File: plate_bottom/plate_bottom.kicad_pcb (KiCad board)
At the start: 2 copper layers, 178.4 x 118.1 mm, 12 parts

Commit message: WIP
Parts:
- moved HM5 2.92 mm to (95.5, 95.7)
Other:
- outline, holes or cut-outs redrawn
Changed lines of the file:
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@@
   (general
     (thickness 1.6)
-    (drawings 117)
+    (drawings 119)
     (tracks 0)
     (zones 0)
@@
   )
   (module used_footprints:Hole_Mount_M4 (layer F.Cu)
+    (at 95.45 95.65)
+    (fp_text reference HM5 (at -0.01 -2.09) (layer Dwgs.User) hide
+      (effects (font (size 1 1) (thickness 0.15)))
+    )
+    (fp_text value CaseHole (at 0.5 -3.77) (layer F.Fab) hide
+      (effects (font (size 1 1) (thickness 0.15)))
+    )
+    (pad "" np_thru_hole circle (at 0 0.08168) (size 2.2 2.2) (drill 2.2) (layers *.Cu *.Mask))
+  )
+  (module used_footprints:Hole_Mount_M4 (layer F.Cu)
     (at 215.4 123.65 36)
     (fp_text reference HM1 (at -0.01 -2.09 36) (layer F.SilkS) hide
@@
   )
   (module used_footprints:Hole_Mount_M4 (layer F.Cu)
-    (at 95.5 98.56832)
-    (fp_text reference HM5 (at -0.01 -2.09) (layer Dwgs.User) hide
-      (effects (font (size 1 1) (thickness 0.15)))
-    )
-    (fp_text value CaseHole (at 0.5 -3.77) (layer F.Fab) hide
-      (effects (font (size 1 1) (thickness 0.15)))
-    )
-    (pad "" np_thru_hole circle (at 0 0.08168) (size 2.2 2.2) (drill 2.2) (layers *.Cu *.Mask))
-  )
-  (module used_footprints:Hole_Mount_M4 (layer F.Cu)
     (at 191.2725 55.183451 14.5)
     (fp_text reference HM2 (at -0.01 -2.09 14.5) (layer Dwgs.User) hide
@@
     (pad "" np_thru_hole circle (at 0 0) (size 2.2 2.2) (drill 2.2) (layers *.Cu *.Mask))
   )
+  (gr_arc (start 77.55 83.01) (end 77.55 82.01) (angle -90) (layer Edge.Cuts) (width 0.05))
+  (gr_arc (start 93.600001 83.01) (end 94.600001 83.01) (angle -90) (layer Edge.Cuts) (width 0.05))
+  (gr_line (start 93.6 100.84) (end 77.55 100.84) (layer Edge.Cuts) (width 0.05))
+  (gr_line (start 77.55 82.01) (end 93.600001 82.01) (layer Edge.Cuts) (width 0.05))
+  (gr_arc (start 77.55 99.84) (end 76.55 99.84) (angle -90) (layer Edge.Cuts) (width 0.05))
+  (gr_line (start 94.600001 83.01) (end 94.600001 84) (layer Edge.Cuts) (width 0.05))
+  (gr_line (start 76.55 99.84) (end 76.55 83.01) (layer Edge.Cuts) (width 0.05))
+  (gr_arc (start 95.099999 86.99) (end 95.599997 86.99) (angle -180) (layer Edge.Cuts) (width 0.05))
+  (gr_line (start 94.600001 92.589999) (end 94.600001 86.99) (layer Edge.Cuts) (width 0.05))
+  (gr_line (start 95.6 86.99) (end 95.599999 92.590001) (layer Edge.Cuts) (width 0.05))
+  (gr_arc (start 95.1 92.59) (end 94.600001 92.589999) (angle -180) (layer Edge.Cuts) (width 0.05))
+  (gr_arc (start 95.1 84) (end 94.600001 84) (angle -180) (layer Edge.Cuts) (width 0.05))
+  (gr_arc (start 93.6 99.84) (end 93.6 100.84) (angle -90) (layer Edge.Cuts) (width 0.05))
+  (gr_arc (start 95.1 98.84) (end 95.6 98.85) (angle -182.2915257) (layer Edge.Cuts) (width 0.05))
+  (gr_line (start 94.6 99.84) (end 94.6 98.85) (layer Edge.Cuts) (width 0.05))
   (gr_line (start 247.677579 53.038559) (end 227.4 56.25) (layer Edge.Cuts) (width 0.05))
   (gr_line (start 249.965825 54.701067) (end 254.95 86.2) (layer Edge.Cuts) (width 0.05))
@@
   (gr_line (start 234.283043 134.070973) (end 223.996802 148.22877) (layer Edge.Cuts) (width 0.05))
   (gr_line (start 96.6 117.55) (end 139.35 117.55) (layer Edge.Cuts) (width 0.05))
-  (gr_arc (start 95.500338 98.622885) (end 93.15 100.8) (angle -48.97400321) (layer Edge.Cuts) (width 0.05))
   (gr_line (start 134.05 52.950001) (end 141.35 52.950001) (layer Edge.Cuts) (width 0.05))
   (gr_line (start 133.05 53.950001) (end 133.05 59.5) (layer Edge.Cuts) (width 0.05))
@@
   (gr_line (start 170.55 30.55) (end 153.75 30.55) (layer Edge.Cuts) (width 0.05))
   (gr_line (start 152.75 31.55) (end 152.75 33.54) (layer Edge.Cuts) (width 0.05))
-  (gr_line (start 95.6 62) (end 95.599999 83.97) (layer Edge.Cuts) (width 0.05))
-  (gr_line (start 94.600001 82.97) (end 94.600001 83.97) (layer Edge.Cuts) (width 0.05))
-  (gr_line (start 76.55 99.8) (end 76.55 82.97) (layer Edge.Cuts) (width 0.05))
-  (gr_line (start 77.55 81.97) (end 93.600001 81.97) (layer Edge.Cuts) (width 0.05))
-  (gr_line (start 95.600014 101.825069) (end 95.6 116.55) (layer Edge.Cuts) (width 0.05))
+  (gr_line (start 95.6 62) (end 95.600099 84) (layer Edge.Cuts) (width 0.05))
+  (gr_line (start 95.6 98.85) (end 95.6 116.55) (layer Edge.Cuts) (width 0.05))
   (gr_arc (start 96.6 116.55) (end 95.6 116.55) (angle -90) (layer Edge.Cuts) (width 0.05))
-  (gr_arc (start 77.55 99.8) (end 76.55 99.8) (angle -90) (layer Edge.Cuts) (width 0.05))
-  (gr_arc (start 77.55 82.97) (end 77.55 81.97) (angle -90) (layer Edge.Cuts) (width 0.05))
-  (gr_arc (start 93.600001 82.97) (end 94.600001 82.97) (angle -90) (layer Edge.Cuts) (width 0.05))
   (gr_arc (start 96.6 42.59) (end 96.6 41.59) (angle -90) (layer Edge.Cuts) (width 0.05))
   (gr_arc (start 132.7 40.59) (end 132.7 41.59) (angle -90) (layer Edge.Cuts) (width 0.05))
@@
   (gr_arc (start 145.35 53.45) (end 145.35 52.950001) (angle -180) (layer Edge.Cuts) (width 0.05))
   (gr_arc (start 141.35 53.449999) (end 141.35 53.949997) (angle -180) (layer Edge.Cuts) (width 0.05))
-  (gr_arc (start 95.1 83.97) (end 94.600001 83.97) (angle -180) (layer Edge.Cuts) (width 0.05))
   (gr_arc (start 134.05 53.950001) (end 134.05 52.950001) (angle -90) (layer Edge.Cuts) (width 0.05))
   (gr_arc (start 153.6 50.45) (end 153.6 49.950001) (angle -90) (layer Edge.Cuts) (width 0.05))
@@
   (gr_line (start 96.6 60) (end 103.25 60.000001) (layer Edge.Cuts) (width 0.05))
   (gr_line (start 103.25 61) (end 96.6 61.000001) (layer Edge.Cuts) (width 0.05))
-  (gr_arc (start 95.099999 86.95) (end 95.599997 86.95) (angle -180) (layer Edge.Cuts) (width 0.05))
-  (gr_line (start 94.6 95.05) (end 94.600001 86.95) (layer Edge.Cuts) (width 0.05))
-  (gr_line (start 95.6 86.95) (end 95.599999 95.05) (layer Edge.Cuts) (width 0.05))
-  (gr_arc (start 95.1 95.049999) (end 94.600001 95.049998) (angle -180) (layer Edge.Cuts) (width 0.05))
-  (gr_line (start 93.15 100.8) (end 77.55 100.8) (layer Edge.Cuts) (width 0.05))
   (gr_line (start 227.4 56.25) (end 209.65 56.25) (layer Edge.Cuts) (width 0.05))
   (gr_line (start 191.7 55.25) (end 199 55.25) (layer Edge.Cuts) (width 0.05))

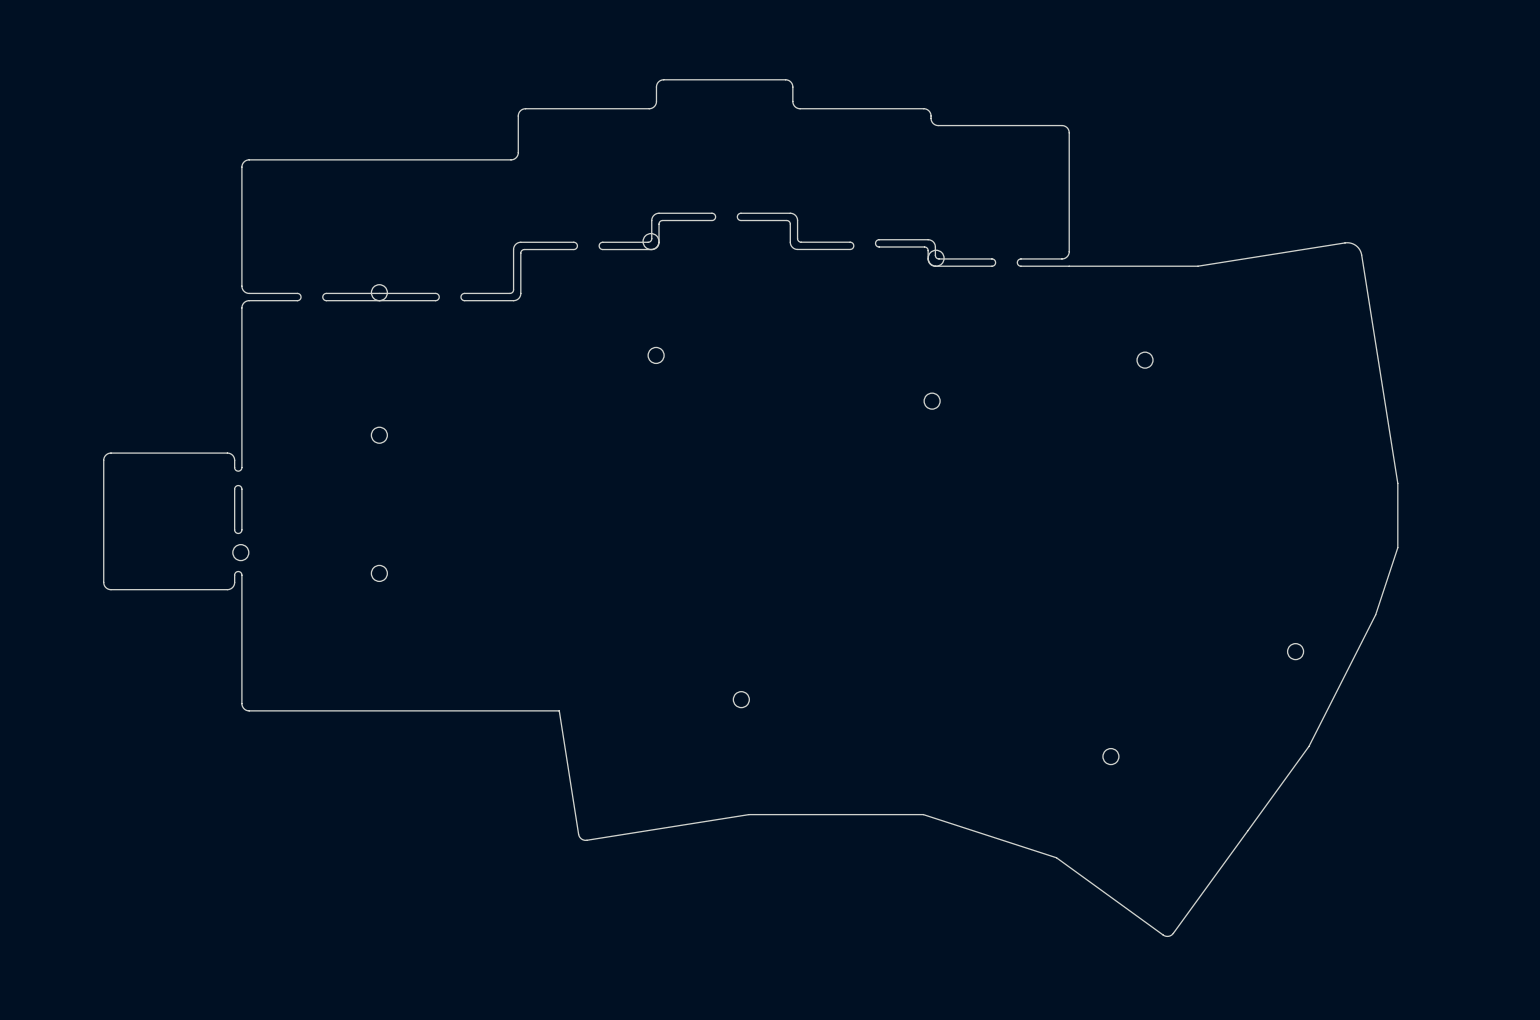
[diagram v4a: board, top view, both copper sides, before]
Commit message: Fixed cut edges + filled zones on plates.
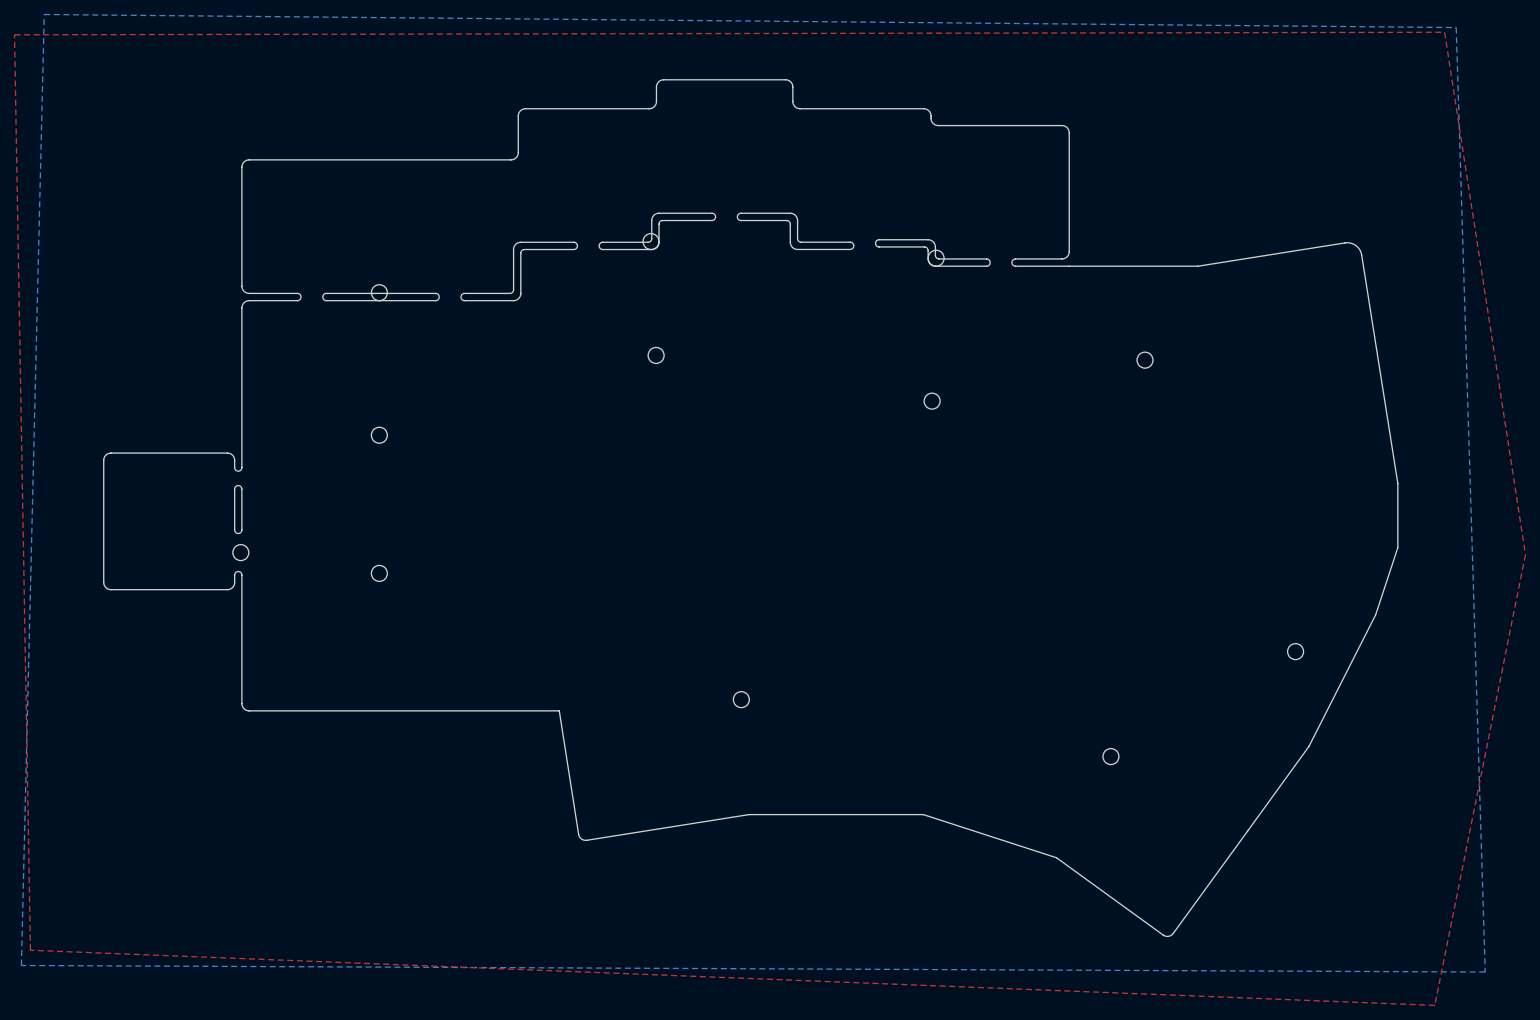
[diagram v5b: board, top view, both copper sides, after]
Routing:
- added copper zone on B.Cu, net (none)
- added copper zone on F.Cu, net (none)
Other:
- outline, holes or cut-outs redrawn
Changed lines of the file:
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@@
     (pad "" np_thru_hole circle (at 0 0) (size 2.2 2.2) (drill 2.2) (layers *.Cu *.Mask))
   )
+  (gr_line (start 191.2 56.25) (end 198.25 56.25) (layer Edge.Cuts) (width 0.05))
+  (gr_arc (start 202.25 55.749999) (end 202.25 55.25) (angle -180) (layer Edge.Cuts) (width 0.05))
+  (gr_arc (start 198.25 55.749998) (end 198.25 56.249996) (angle -180) (layer Edge.Cuts) (width 0.05))
+  (gr_line (start 191.7 55.25) (end 198.25 55.25) (layer Edge.Cuts) (width 0.05))
+  (gr_line (start 208.65 55.25) (end 202.25 55.25) (layer Edge.Cuts) (width 0.05))
   (gr_arc (start 77.55 83.01) (end 77.55 82.01) (angle -90) (layer Edge.Cuts) (width 0.05))
   (gr_arc (start 93.600001 83.01) (end 94.600001 83.01) (angle -90) (layer Edge.Cuts) (width 0.05))
@@
   (gr_line (start 183.45 53.6) (end 189.7 53.6) (layer Edge.Cuts) (width 0.05))
   (gr_line (start 190.2 54.1) (end 190.2 55.25) (layer Edge.Cuts) (width 0.05))
-  (gr_line (start 191.2 56.25) (end 199 56.249996) (layer Edge.Cuts) (width 0.05))
   (gr_line (start 209.65 54.25) (end 209.65 37.86) (layer Edge.Cuts) (width 0.05))
   (gr_line (start 208.65 36.86) (end 191.6 36.86) (layer Edge.Cuts) (width 0.05))
@@
   (gr_line (start 165.5 131.85) (end 189.55 131.85) (layer Edge.Cuts) (width 0.05))
   (gr_arc (start 134.55 54.449999) (end 134.55 53.95) (angle -90) (layer Edge.Cuts) (width 0.05))
-  (gr_line (start 203 56.249998) (end 209.65 56.25) (layer Edge.Cuts) (width 0.05))
-  (gr_line (start 208.65 55.25) (end 203 55.25) (layer Edge.Cuts) (width 0.05))
+  (gr_line (start 202.25 56.249998) (end 209.65 56.25) (layer Edge.Cuts) (width 0.05))
   (gr_arc (start 133.05 59.999999) (end 133.05 60.999999) (angle -90) (layer Edge.Cuts) (width 0.05))
   (gr_arc (start 122.3 60.499999) (end 122.3 60.999997) (angle -180) (layer Edge.Cuts) (width 0.05))
@@
   (gr_line (start 103.25 61) (end 96.6 61.000001) (layer Edge.Cuts) (width 0.05))
   (gr_line (start 227.4 56.25) (end 209.65 56.25) (layer Edge.Cuts) (width 0.05))
-  (gr_line (start 191.7 55.25) (end 199 55.25) (layer Edge.Cuts) (width 0.05))
-  (gr_arc (start 199 55.749998) (end 199 56.249996) (angle -180) (layer Edge.Cuts) (width 0.05))
-  (gr_arc (start 203 55.749999) (end 203 55.25) (angle -180) (layer Edge.Cuts) (width 0.05))
+  (zone (net 0) (net_name "") (layer F.Cu) (hatch edge 0.508)
+    (connect_pads (clearance 0.508))
+    (min_thickness 0.254)
+    (fill yes (arc_segments 32) (thermal_gap 0.508) (thermal_bridge_width 0.508))
+    (polygon
+      (pts
+        (xy 272.55 96) (xy 260.05 158.15) (xy 66.45 150.55) (xy 64.25 24.35) (xy 261.4 24)
+      )
+    )
+  )
+  (zone (net 0) (net_name "") (layer B.Cu) (hatch edge 0.508)
+    (connect_pads (clearance 0.508))
+    (min_thickness 0.254)
+    (fill yes (arc_segments 32) (thermal_gap 0.508) (thermal_bridge_width 0.508))
+    (polygon
+      (pts
+        (xy 263 23.35) (xy 267 153.55) (xy 65.2 152.65) (xy 68.35 21.55)
+      )
+    )
+  )
 )

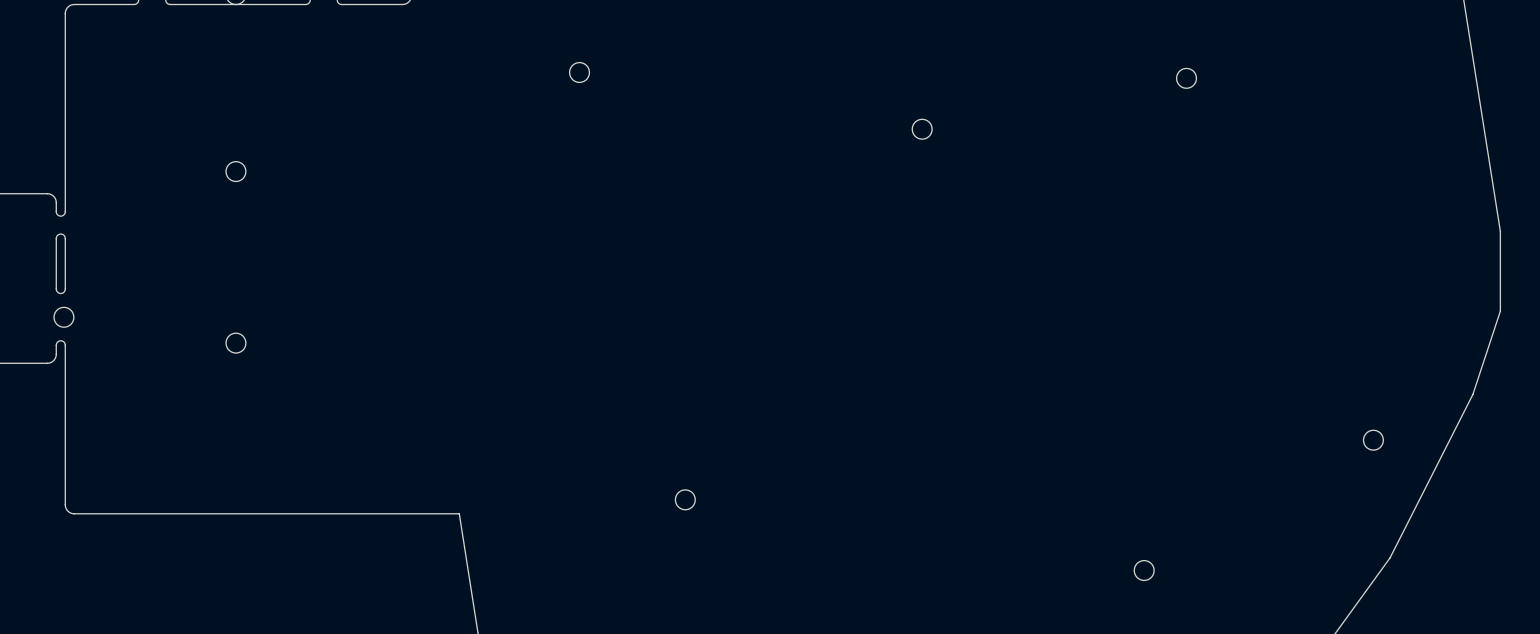
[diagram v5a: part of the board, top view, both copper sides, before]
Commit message: Added dimensions.
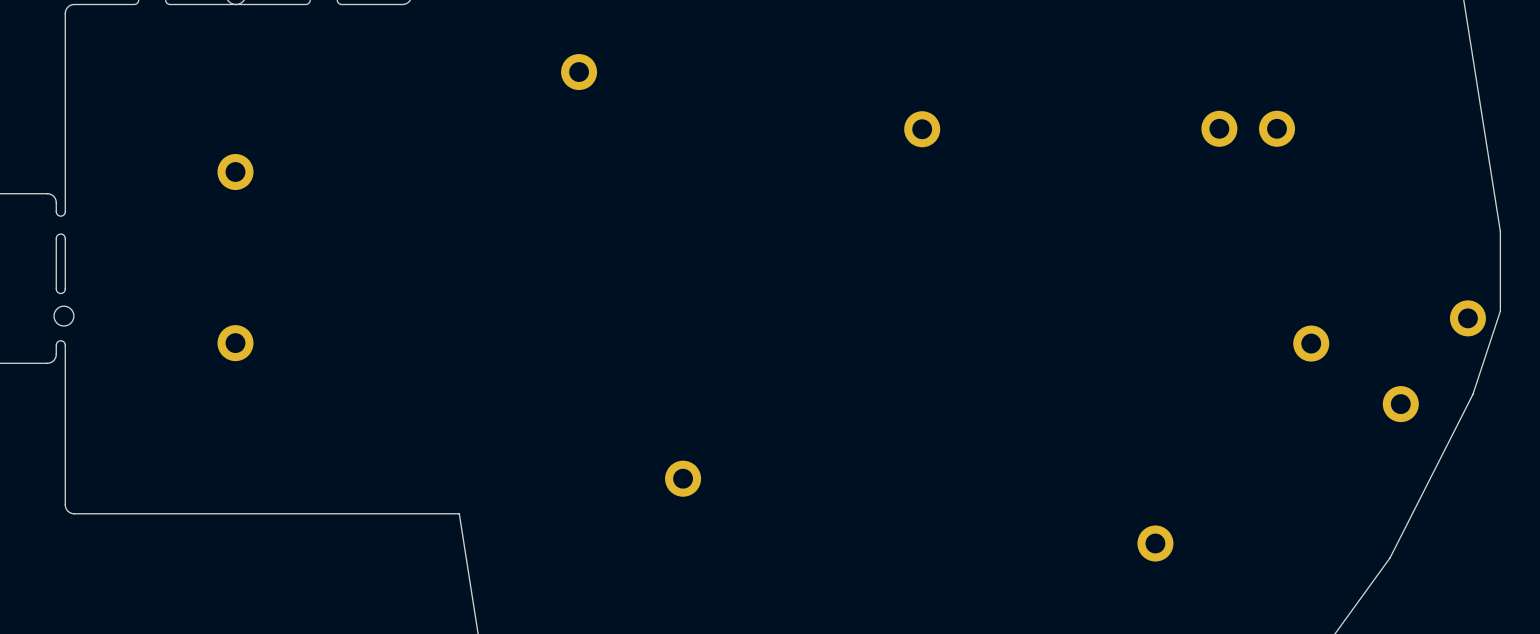
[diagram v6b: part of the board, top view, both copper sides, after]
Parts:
- added H13: MountingHole, used_footprints:M2_HOLE_PCB, F.Cu at (233.9, 98.7)
- added H15: MountingHole, used_footprints:M2_HOLE_PCB, F.Cu at (251.3, 95.8)
- added H16: MountingHole, used_footprints:M2_HOLE_PCB, F.Cu at (230.2, 74.8)
- HM1, HM10, HM11, HM12, HM2, HM3, HM4, HM5, HM6, HM7, HM8, HM9: footprint used_footprints:Hole_Mount_M4 -> used_footprints:M2_HOLE_PCB
- moved HM12 6.68 mm to (223.8, 74.8)
- moved HM3 5.13 mm to (243.9, 105.4)
- moved HM1 3.07 mm to (216.7, 120.8), turned to 0 degrees
- moved HM4 3.06 mm to (164.2, 113.7)
- moved HM9 0.82 mm to (152.0, 52.9)
- moved HM6 0.14 mm to (114.5, 98.6)
- moved HM8 0.07 mm to (114.5, 79.6)
- moved HM11 0.07 mm to (152.7, 68.5)
- moved HM5 0.05 mm to (95.5, 95.6)
